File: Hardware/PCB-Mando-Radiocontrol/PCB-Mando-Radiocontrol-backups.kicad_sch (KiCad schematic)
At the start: 25 parts, among them J2 ALIMENTACION, J3 USB 2.0 a UART TTL 6 pines CP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, SW1 SW_SPDT, SW2 SW_SPDT, SW3 SW_SPDT, U1 ATMEGA328P, U2 Nrf24l01, U3 AMS1117-3.3, U4 AMS1117-5.0, U5 COM-09032, U6 COM-09032, Y1 16MHZ

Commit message: SCH completo, PCB en proceso ~90% completado
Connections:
- net GND: no longer U5.S1 (SHIELD), U5.S2 (SHIELD), U5.S3 (SHIELD), U5.S4 (SHIELD), U6.S1 (SHIELD), U6.S2 (SHIELD), U6.S3 (SHIELD), U6.S4 (SHIELD)
- new net: U5.S1 (SHIELD), U5.S2 (SHIELD), U5.S3 (SHIELD), U5.S4 (SHIELD)
- new net: U6.S1 (SHIELD), U6.S2 (SHIELD), U6.S3 (SHIELD), U6.S4 (SHIELD)
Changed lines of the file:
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@@
   (junction (at 31.75 46.99) (diameter 0) (color 0 0 0 0)
   )
-  (junction (at 242.57 54.61) (diameter 0) (color 0 0 0 0)
-  )
   (junction (at 60.96 73.66) (diameter 0) (color 0 0 0 0)
   )
@@
   (junction (at 165.1 91.186) (diameter 0) (color 0 0 0 0)
   )
-  (junction (at 196.85 54.61) (diameter 0) (color 0 0 0 0)
-  )
   (junction (at 60.96 109.728) (diameter 0) (color 0 0 0 0)
   )
@@
     (stroke (width 0) (type default))
   )
-  (wire (pts (xy 196.85 54.61) (xy 201.93 54.61))
-    (stroke (width 0) (type default))
-  )
   (wire (pts (xy 31.75 46.99) (xy 43.18 46.99))
     (stroke (width 0) (type default))
@@
     (stroke (width 0) (type default))
   )
-  (wire (pts (xy 196.85 49.53) (xy 196.85 54.61))
-    (stroke (width 0) (type default))
-  )
   (wire (pts (xy 121.92 91.44) (xy 106.68 91.44))
     (stroke (width 0) (type default))
@@
     (stroke (width 0) (type default))
   )
-  (wire (pts (xy 196.85 54.61) (xy 196.85 58.42))
+  (wire (pts (xy 196.85 49.53) (xy 196.85 58.42))
     (stroke (width 0) (type default))
   )
@@
     (stroke (width 0) (type default))
   )
-  (wire (pts (xy 242.57 54.61) (xy 242.57 58.42))
-    (stroke (width 0) (type default))
-  )
   (wire (pts (xy 237.49 33.02) (xy 237.49 36.83))
     (stroke (width 0) (type default))
@@
     (stroke (width 0) (type dash))
   )
-  (wire (pts (xy 242.57 49.53) (xy 242.57 54.61))
+  (wire (pts (xy 242.57 49.53) (xy 242.57 58.42))
     (stroke (width 0) (type default))
   )
@@
     (stroke (width 0) (type default))
   )
-  (wire (pts (xy 242.57 54.61) (xy 247.65 54.61))
-    (stroke (width 0) (type default))
-  )

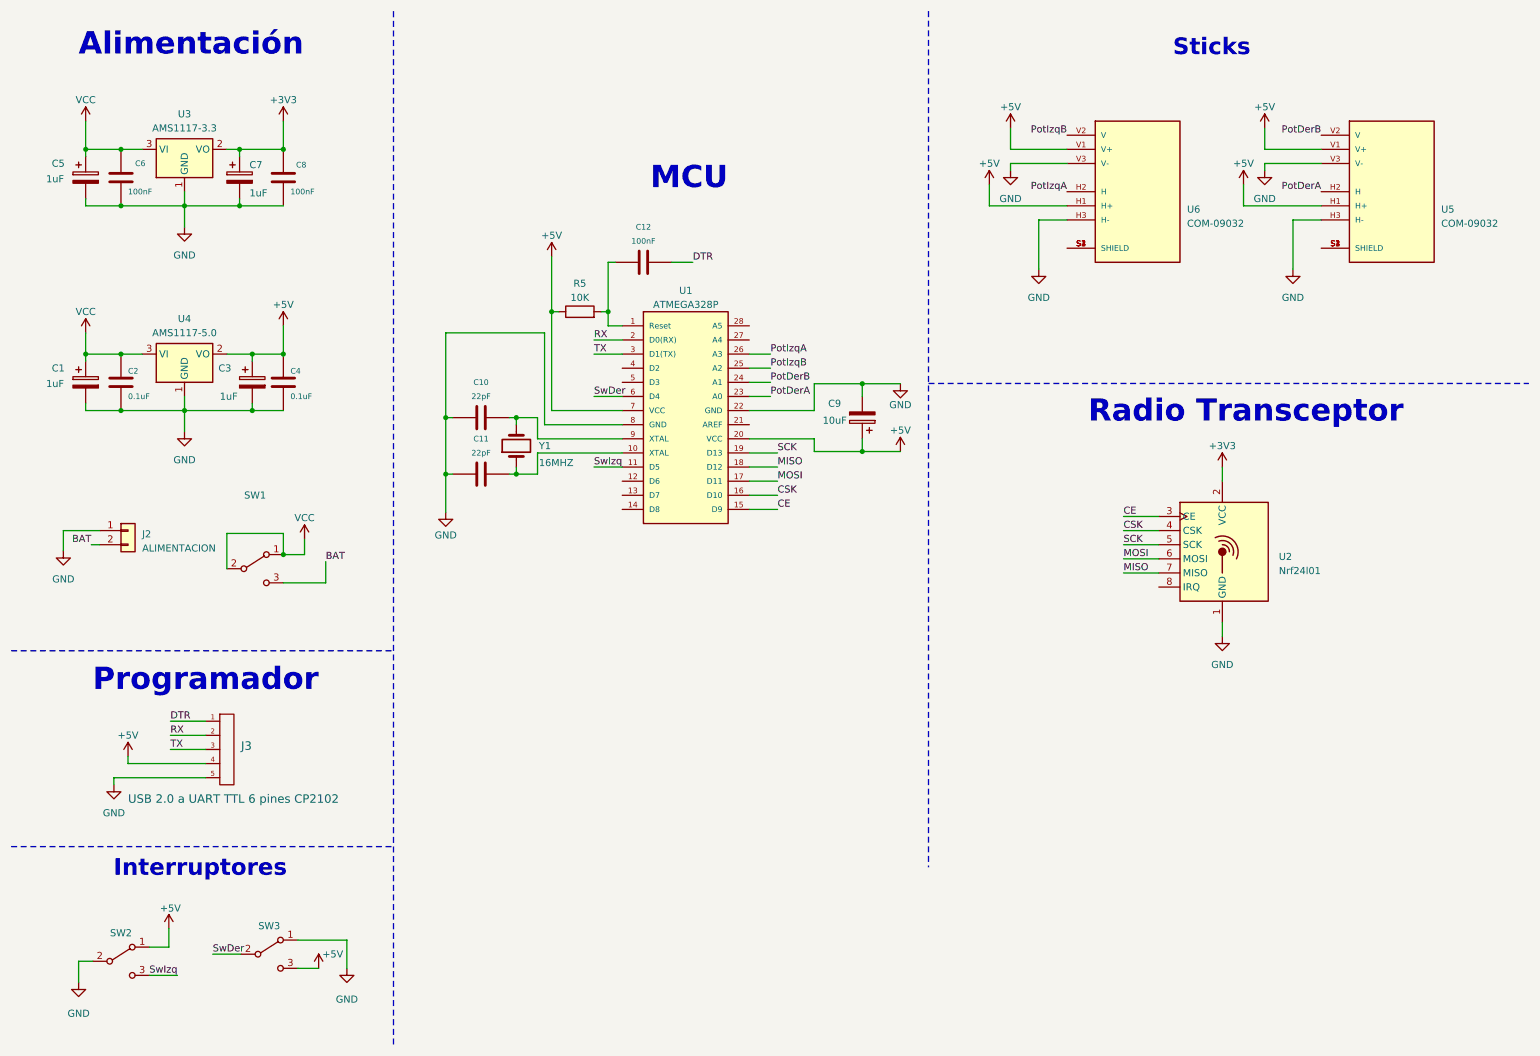
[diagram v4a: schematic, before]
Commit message: realice modificaciones desde 0 en el PCB a continuar por leandro, es una placa en paralelo a la de gabi
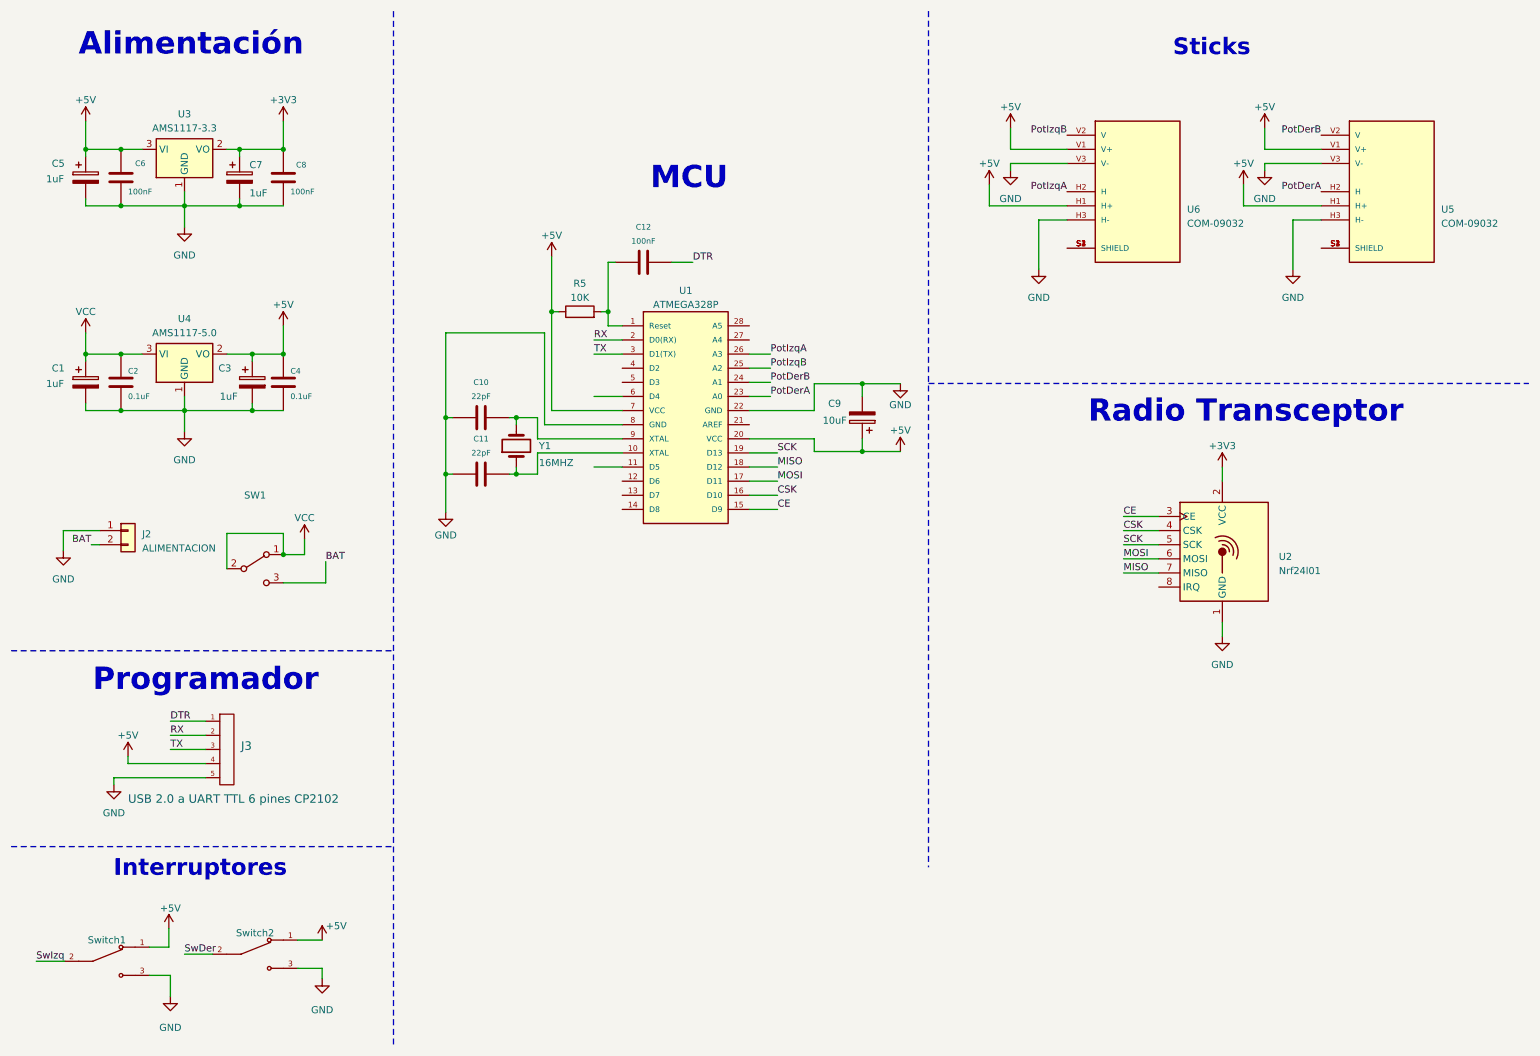
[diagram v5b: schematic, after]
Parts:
- removed SW2, SW3: SW_SPDT, EESTN5:Pin_Header_3, symbol EESTN5:SW_SPDT
- added Switch1, Switch2: ~, Footprints:SW_100SP3T1B1M2QE, symbol Librerias:Switch
- SW1: footprint EESTN5:Pin_Header_3 -> Footprints:SW_100SP3T1B1M2QE
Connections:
- net +5V: now also C5.1, C6.1, U3.3 (VI), Switch1.1, Switch2.1
- net GND: now also Switch1.3, Switch2.3
- net SwDer: now also Switch2.2; no longer U1.6 (D4)
- net SwIzq: now also Switch1.2; no longer U1.11 (D5)
- net VCC: no longer C5.1, C6.1, U3.3 (VI)

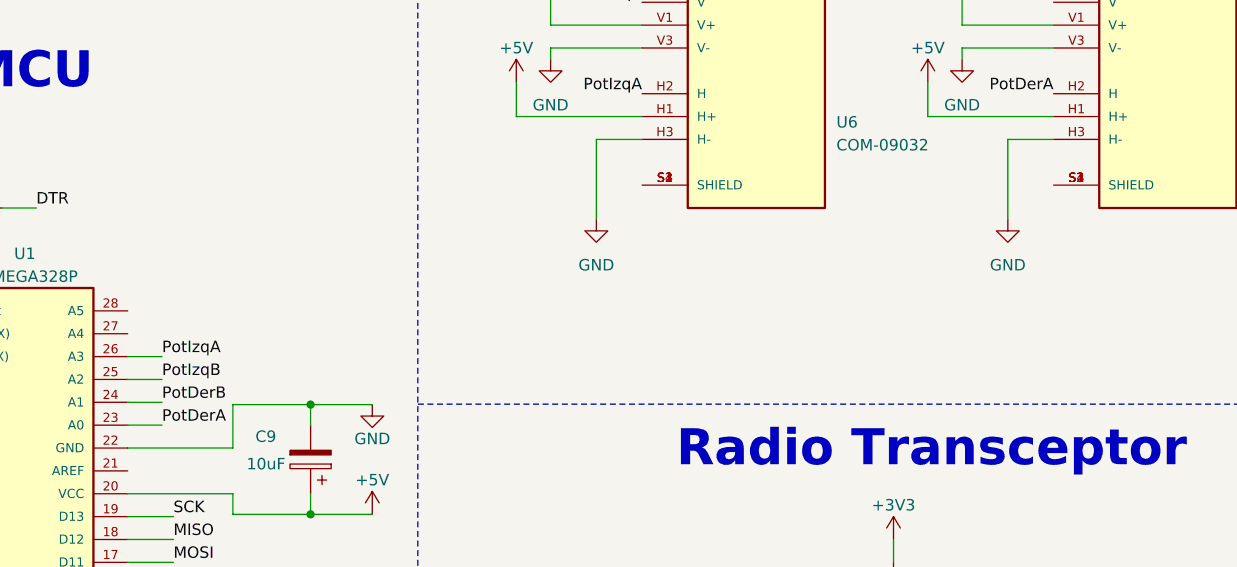
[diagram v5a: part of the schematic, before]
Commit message: realice la base final de la placa , ordene cosas y cambie pines me falta agregar dos switches y ordenar y corroborar todo
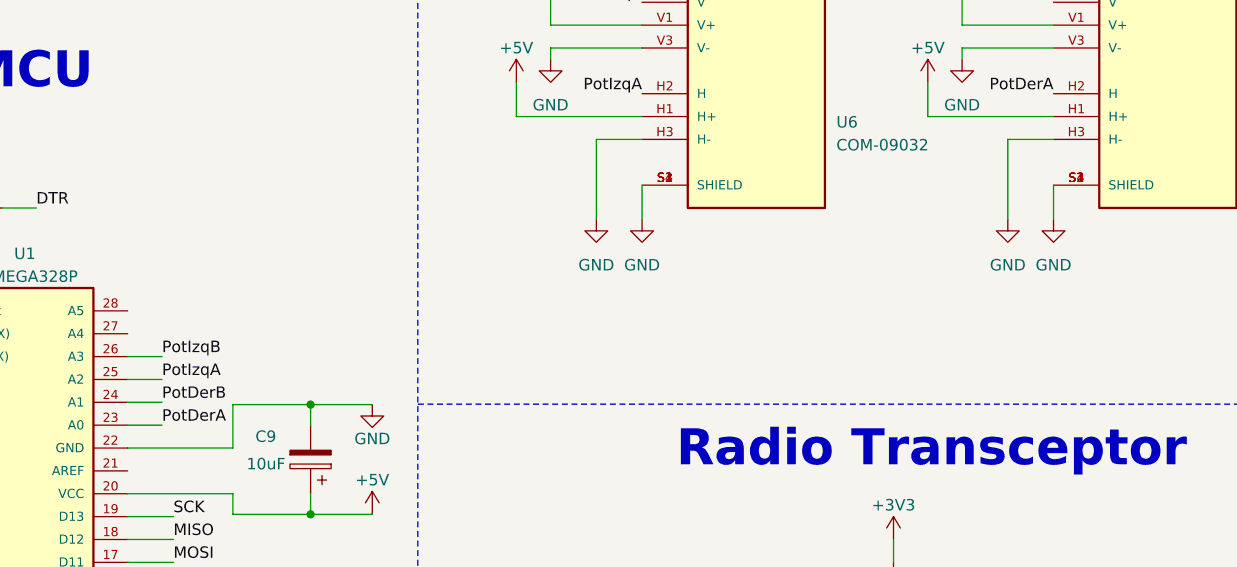
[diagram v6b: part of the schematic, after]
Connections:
- net GND: now also U5.S1 (SHIELD), U5.S2 (SHIELD), U5.S3 (SHIELD), U5.S4 (SHIELD), U6.S1 (SHIELD), U6.S2 (SHIELD), U6.S3 (SHIELD), U6.S4 (SHIELD)
- net PotIzqA: now also U1.25 (A2); no longer U1.26 (A3)
- net PotIzqB: now also U1.26 (A3); no longer U1.25 (A2)
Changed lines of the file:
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@@
     (stroke (width 0) (type default))
   )
+  (wire (pts (xy 201.93 54.61) (xy 201.93 58.42))
+    (stroke (width 0) (type default))
+  )
   (wire (pts (xy 109.22 66.04) (xy 110.49 66.04))
     (stroke (width 0) (type default))
@@
     (stroke (width 0) (type default))
   )
+  (wire (pts (xy 247.65 54.61) (xy 247.65 58.42))
+    (stroke (width 0) (type default))
+  )
   (wire (pts (xy 90.17 69.85) (xy 90.17 85.09))
     (stroke (width 0) (type default))
@@
     (effects (font (size 1.27 1.27)) (justify right bottom))
   )
-  (label "PotIzqA" (at 148.59 73.66 0) (fields_autoplaced)
-    (effects (font (size 1.27 1.27)) (justify left bottom))
-  )
   (label "CSK" (at 149.86 99.06 0) (fields_autoplaced)
     (effects (font (size 1.27 1.27)) (justify left bottom))
@@
     (effects (font (size 1.27 1.27)) (justify left bottom))
   )
-  (label "PotIzqB" (at 148.59 76.2 0) (fields_autoplaced)
-    (effects (font (size 1.27 1.27)) (justify left bottom))
-  )
   (label "MISO" (at 212.09 113.03 0) (fields_autoplaced)
     (effects (font (size 1.27 1.27)) (justify left bottom))
@@
     (effects (font (size 1.27 1.27)) (justify left bottom))
   )
+  (label "PotIzqB" (at 148.59 73.66 0) (fields_autoplaced)
+    (effects (font (size 1.27 1.27)) (justify left bottom))
+  )
   (label "BAT" (at 68.58 110.998 0) (fields_autoplaced)
     (effects (font (size 1.27 1.27)) (justify left bottom))
@@
     (effects (font (size 1.27 1.27)) (justify right bottom))
   )
+  (label "PotIzqA" (at 148.59 76.2 0) (fields_autoplaced)
+    (effects (font (size 1.27 1.27)) (justify left bottom))
+  )
   (label "DTR" (at 40.64 139.7 0) (fields_autoplaced)
     (effects (font (size 1.27 1.27)) (justify left bottom))
@@
     )
   )
+  (symbol (lib_id "power:GND") (at 201.93 58.42 0) (unit 1)
+    (in_bom yes) (on_board yes) (dnp no) (fields_autoplaced)
+    (property "Reference" "#PWR021" (at 201.93 64.77 0)
+      (effects (font (size 1.27 1.27)) hide)
+    )
+    (property "Value" "GND" (at 201.93 63.5 0)
+      (effects (font (size 1.27 1.27)))
+    )
+    (property "Footprint" "" (at 201.93 58.42 0)
+      (effects (font (size 1.27 1.27)) hide)
+    )
+    (property "Datasheet" "" (at 201.93 58.42 0)
+      (effects (font (size 1.27 1.27)) hide)
+    )
+    (pin "1")
+    (instances
+      (project "PCB-Mando-Radiocontrol-backups"
+        (path "/a09d701e-8048-4e72-8e3a-cb0f8f921380"
+          (reference "#PWR021") (unit 1)
+        )
+      )
+    )
+  )
   (symbol (lib_id "Device:C_Polarized") (at 53.086 41.91 0) (unit 1)
     (in_bom yes) (on_board yes) (dnp no)
@@
         )
       )
+    )
+  )
+  (symbol (lib_id "power:GND") (at 247.65 58.42 0) (unit 1)
+    (in_bom yes) (on_board yes) (dnp no) (fields_autoplaced)
+    (property "Reference" "#PWR014" (at 247.65 64.77 0)
+      (effects (font (size 1.27 1.27)) hide)
+    )
+    (property "Value" "GND" (at 247.65 63.5 0)
+      (effects (font (size 1.27 1.27)))
+    )
+    (property "Footprint" "" (at 247.65 58.42 0)
+      (effects (font (size 1.27 1.27)) hide)
+    )
+    (property "Datasheet" "" (at 247.65 58.42 0)
+      (effects (font (size 1.27 1.27)) hide)
+    )
+    (pin "1")
+    (instances
+      (project "PCB-Mando-Radiocontrol-backups"
+        (path "/a09d701e-8048-4e72-8e3a-cb0f8f921380"
+          (reference "#PWR014") (unit 1)
+        )
+      )
